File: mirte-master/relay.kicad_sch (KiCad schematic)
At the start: 2 parts, among them J17 NO relay contacts, J19 relay

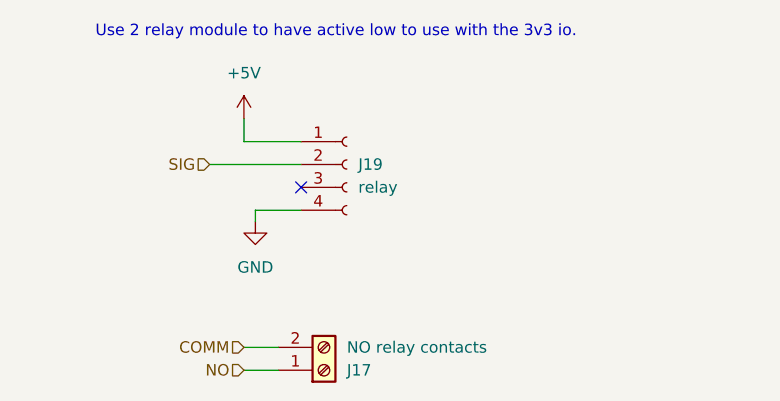
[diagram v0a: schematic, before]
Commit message: add kerco/elcos
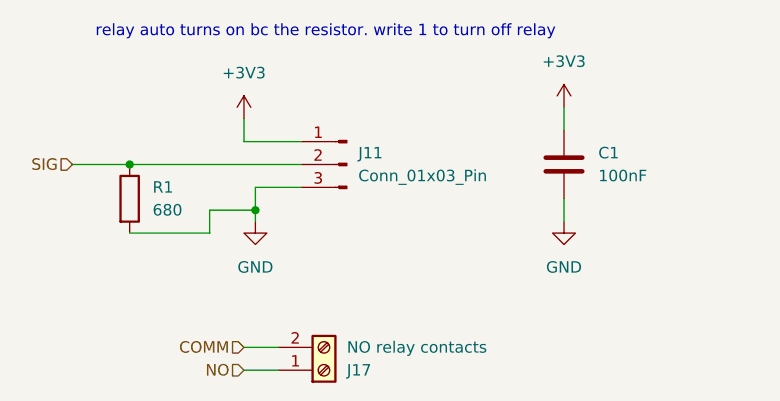
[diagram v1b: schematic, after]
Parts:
- removed J19: relay, Connector_JST:JST_XH_B4B-XH-A_1x04_P2.50mm_Vertical, symbol Connector:Conn_01x04_Socket
- added C1: 100nF, Capacitor_SMD:C_0805_2012Metric, symbol Device:C
- added J11: Conn_01x03_Pin, Connector_PinHeader_2.54mm:PinHeader_1x03_P2.54mm_Vertical, symbol Connector:Conn_01x03_Pin
- added R1: 680, Resistor_SMD:R_0805_2012Metric, symbol Device:R
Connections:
- net GND: now also C1.2, J11.3 (Pin_3), R1.2
- net SIG: now also J11.2 (Pin_2), R1.1
- new net +3V3: C1.1, J11.1 (Pin_1)
- no-connect marks 1 -> 0
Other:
- note added: "relay auto turns on bc the resistor. write 1 to turn off relay"
- note removed: "Use 2 relay module to have active low to use with the 3v3 io."
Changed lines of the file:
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@@
 (kicad_sch (version 20230121) (generator eeschema)
   (paper "A4")
-  (no_connect (at 101.6 67.31))
+  (junction (at 82.55 64.77) (diameter 0) (color 0 0 0 0)
+  )
+  (junction (at 96.52 69.85) (diameter 0) (color 0 0 0 0)
+  )
+  (wire (pts (xy 96.52 69.85) (xy 91.44 69.85))
+    (stroke (width 0) (type default))
+  )
   (wire (pts (xy 96.52 71.12) (xy 96.52 69.85))
     (stroke (width 0) (type default))
@@
     (stroke (width 0) (type default))
   )
-  (wire (pts (xy 96.52 69.85) (xy 101.6 69.85))
+  (wire (pts (xy 82.55 64.77) (xy 101.6 64.77))
+    (stroke (width 0) (type default))
+  )
+  (wire (pts (xy 130.81 58.42) (xy 130.81 60.96))
     (stroke (width 0) (type default))
   )
@@
     (stroke (width 0) (type default))
   )
-  (wire (pts (xy 91.44 64.77) (xy 101.6 64.77))
+  (wire (pts (xy 130.81 68.58) (xy 130.81 71.12))
+    (stroke (width 0) (type default))
+  )
+  (wire (pts (xy 91.44 69.85) (xy 91.44 72.39))
+    (stroke (width 0) (type default))
+  )
+  (wire (pts (xy 91.44 72.39) (xy 82.55 72.39))
+    (stroke (width 0) (type default))
+  )
+  (wire (pts (xy 76.2 64.77) (xy 82.55 64.77))
     (stroke (width 0) (type default))
   )
@@
     (stroke (width 0) (type default))
   )
+  (wire (pts (xy 96.52 69.85) (xy 96.52 67.31))
+    (stroke (width 0) (type default))
+  )
   (wire (pts (xy 95.25 85.09) (xy 99.06 85.09))
     (stroke (width 0) (type default))
   )
-  (text "Use 2 relay module to have active low to use with the 3v3 io."
+  (wire (pts (xy 96.52 67.31) (xy 101.6 67.31))
+    (stroke (width 0) (type default))
+  )
+  (text "relay auto turns on bc the resistor. write 1 to turn off relay"
     (at 78.74 50.8 0)
     (effects (font (size 1.27 1.27)) (justify left bottom))
@@
     (effects (font (size 1.27 1.27)) (justify right))
   )
-  (hierarchical_label "SIG" (shape input) (at 91.44 64.77 180) (fields_autoplaced)
+  (hierarchical_label "SIG" (shape input) (at 76.2 64.77 180) (fields_autoplaced)
     (effects (font (size 1.27 1.27)) (justify right))
+  )
+  (symbol (lib_id "Connector:Conn_01x03_Pin") (at 106.68 64.77 0) (mirror y) (unit 1)
+    (in_bom yes) (on_board yes) (dnp no) (fields_autoplaced)
+    (property "Reference" "J11" (at 107.95 63.5 0)
+      (effects (font (size 1.27 1.27)) (justify right))
+    )
+    (property "Value" "Conn_01x03_Pin" (at 107.95 66.04 0)
+      (effects (font (size 1.27 1.27)) (justify right))
+    )
+    (property "Footprint" "Connector_PinHeader_2.54mm:PinHeader_1x03_P2.54mm_Vertical" (at 106.68 64.77 0)
+      (effects (font (size 1.27 1.27)) hide)
+    )
+    (property "Datasheet" "~" (at 106.68 64.77 0)
+      (effects (font (size 1.27 1.27)) hide)
+    )
+    (pin "2")
+    (pin "3")
+    (pin "1")
+    (instances
+      (project "mirte-master"
+        (path "/19794465-0368-488c-958e-83b02754ebd6/17ebe4c8-09bb-4699-976c-396d27e4a3f5/544a16a8-9ef3-43b3-aa0f-4bd972816cae/d3337f2d-26a9-4529-9bfc-380e6deefc08"
+          (reference "J11") (unit 1)
+        )
+      )
+    )
+  )
+  (symbol (lib_id "power:GND") (at 130.81 71.12 0) (unit 1)
+    (in_bom yes) (on_board yes) (dnp no)
+    (property "Reference" "#PWR066" (at 130.81 77.47 0)
+      (effects (font (size 1.27 1.27)) hide)
+    )
+    (property "Value" "GND" (at 130.81 76.2 0)
+      (effects (font (size 1.27 1.27)))
+    )
+    (property "Footprint" "" (at 130.81 71.12 0)
+      (effects (font (size 1.27 1.27)) hide)
+    )
+    (property "Datasheet" "" (at 130.81 71.12 0)
+      (effects (font (size 1.27 1.27)) hide)
+    )
+    (pin "1")
+    (instances
+      (project "mirte-master"
+        (path "/19794465-0368-488c-958e-83b02754ebd6/17ebe4c8-09bb-4699-976c-396d27e4a3f5/544a16a8-9ef3-43b3-aa0f-4bd972816cae/d3337f2d-26a9-4529-9bfc-380e6deefc08"
+          (reference "#PWR066") (unit 1)
+        )
+      )
+    )
+  )
+  (symbol (lib_id "Device:C") (at 130.81 64.77 0) (unit 1)
+    (in_bom yes) (on_board yes) (dnp no) (fields_autoplaced)
+    (property "Reference" "C1" (at 134.62 63.5 0)
+      (effects (font (size 1.27 1.27)) (justify left))
+    )
+    (property "Value" "100nF" (at 134.62 66.04 0)
+      (effects (font (size 1.27 1.27)) (justify left))
+    )
+    (property "Footprint" "Capacitor_SMD:C_0805_2012Metric" (at 131.7752 68.58 0)
+      (effects (font (size 1.27 1.27)) hide)
+    )
+    (property "Datasheet" "~" (at 130.81 64.77 0)
+      (effects (font (size 1.27 1.27)) hide)
+    )
+    (pin "2")
+    (pin "1")
+    (instances
+      (project "mirte-master"
+        (path "/19794465-0368-488c-958e-83b02754ebd6/17ebe4c8-09bb-4699-976c-396d27e4a3f5"
+          (reference "C1") (unit 1)
+        )
+        (path "/19794465-0368-488c-958e-83b02754ebd6/17ebe4c8-09bb-4699-976c-396d27e4a3f5/544a16a8-9ef3-43b3-aa0f-4bd972816cae/d3337f2d-26a9-4529-9bfc-380e6deefc08"
+          (reference "C4") (unit 1)
+        )
+      )
+    )
   )
   (symbol (lib_id "Connector:Screw_Terminal_01x02") (at 104.14 87.63 0) (mirror x) (unit 1)
@@
     )
   )
-  (symbol (lib_id "power:+5V") (at 95.25 59.69 0) (unit 1)
-    (in_bom yes) (on_board yes) (dnp no) (fields_autoplaced)
-    (property "Reference" "#PWR013" (at 95.25 63.5 0)
-      (effects (font (size 1.27 1.27)) hide)
-    )
-    (property "Value" "+5V" (at 95.25 54.61 0)
+  (symbol (lib_id "power:+3V3") (at 95.25 59.69 0) (unit 1)
+    (in_bom yes) (on_board yes) (dnp no) (fields_autoplaced)
+    (property "Reference" "#PWR010" (at 95.25 63.5 0)
+      (effects (font (size 1.27 1.27)) hide)
+    )
+    (property "Value" "+3V3" (at 95.25 54.61 0)
       (effects (font (size 1.27 1.27)))
     )
@@
       (project "mirte-master"
         (path "/19794465-0368-488c-958e-83b02754ebd6/17ebe4c8-09bb-4699-976c-396d27e4a3f5/544a16a8-9ef3-43b3-aa0f-4bd972816cae/d3337f2d-26a9-4529-9bfc-380e6deefc08"
-          (reference "#PWR013") (unit 1)
+          (reference "#PWR010") (unit 1)
         )
       )
@@
     )
   )
-  (symbol (lib_id "Connector:Conn_01x04_Socket") (at 106.68 64.77 0) (unit 1)
-    (in_bom yes) (on_board yes) (dnp no) (fields_autoplaced)
-    (property "Reference" "J19" (at 107.95 64.77 0)
-      (effects (font (size 1.27 1.27)) (justify left))
-    )
-    (property "Value" "relay" (at 107.95 67.31 0)
-      (effects (font (size 1.27 1.27)) (justify left))
-    )
-    (property "Footprint" "Connector_JST:JST_XH_B4B-XH-A_1x04_P2.50mm_Vertical" (at 106.68 64.77 0)
-      (effects (font (size 1.27 1.27)) hide)
-    )
-    (property "Datasheet" "~" (at 106.68 64.77 0)
-      (effects (font (size 1.27 1.27)) hide)
-    )
-    (property "LCSC" "C144395" (at 107.95 64.77 0)
-      (effects (font (size 1.27 1.27)) hide)
-    )
-    (pin "1")
-    (pin "2")
-    (pin "4")
-    (pin "3")
-    (instances
-      (project "mirte-master"
-        (path "/19794465-0368-488c-958e-83b02754ebd6/17ebe4c8-09bb-4699-976c-396d27e4a3f5/544a16a8-9ef3-43b3-aa0f-4bd972816cae/d3337f2d-26a9-4529-9bfc-380e6deefc08"
-          (reference "J19") (unit 1)
-        )
-      )
+  (symbol (lib_id "Device:R") (at 82.55 68.58 0) (unit 1)
+    (in_bom yes) (on_board yes) (dnp no) (fields_autoplaced)
+    (property "Reference" "R1" (at 85.09 67.31 0)
+      (effects (font (size 1.27 1.27)) (justify left))
+    )
+    (property "Value" "680" (at 85.09 69.85 0)
+      (effects (font (size 1.27 1.27)) (justify left))
+    )
+    (property "Footprint" "Resistor_SMD:R_0805_2012Metric" (at 80.772 68.58 90)
+      (effects (font (size 1.27 1.27)) hide)
+    )
+    (property "Datasheet" "~" (at 82.55 68.58 0)
+      (effects (font (size 1.27 1.27)) hide)
+    )
+    (pin "2")
+    (pin "1")
+    (instances
+      (project "mirte-master"
+        (path "/19794465-0368-488c-958e-83b02754ebd6/17ebe4c8-09bb-4699-976c-396d27e4a3f5/544a16a8-9ef3-43b3-aa0f-4bd972816cae/d3337f2d-26a9-4529-9bfc-380e6deefc08"
+          (reference "R1") (unit 1)
+        )
+      )
+    )
+  )
+  (symbol (lib_id "power:+3V3") (at 130.81 58.42 0) (unit 1)
+    (in_bom yes) (on_board yes) (dnp no) (fields_autoplaced)
+    (property "Reference" "#PWR065" (at 130.81 62.23 0)
+      (effects (font (size 1.27 1.27)) hide)
+    )
+    (property "Value" "+3V3" (at 130.81 53.34 0)
+      (effects (font (size 1.27 1.27)))
+    )
+    (property "Footprint" "" (at 130.81 58.42 0)
+      (effects (font (size 1.27 1.27)) hide)
+    )
+    (property "Datasheet" "" (at 130.81 58.42 0)
+      (effects (font (size 1.27 1.27)) hide)
+    )
+    (pin "1")
+    (instances
+      (project "mirte-master"
+        (path "/19794465-0368-488c-958e-83b02754ebd6/17ebe4c8-09bb-4699-976c-396d27e4a3f5/544a16a8-9ef3-43b3-aa0f-4bd972816cae/d3337f2d-26a9-4529-9bfc-380e6deefc08"
+          (reference "#PWR065") (unit 1)
+        )
+      )

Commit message: mirte master parts jclpcb fixed
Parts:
- removed J17: NO relay contacts, TerminalBlock_Phoenix:TerminalBlock_Phoenix_PT-1,5-2-5.0-H_1x02_P5.00mm_Horizontal, symbol Connector:Screw_Terminal_01x02
- added J23: sc, easyeda:CONN-TH_XY126V-5.0-2P, symbol Connector:Screw_Terminal_01x02
- C1: LCSC (none) -> C49678
- J11: footprint Connector_PinHeader_2.54mm:PinHeader_1x03_P2.54mm_Vertical -> Connector_JST:JST_XH_B3B-XH-A_1x03_P2.50mm_Vertical; LCSC (none) -> C144394
- R1: LCSC (none) -> C17798
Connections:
- net COMM: now also J23.1 (Pin_1)
- net NO: now also J23.2 (Pin_2)
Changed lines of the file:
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@@
       (effects (font (size 1.27 1.27)) (justify right))
     )
-    (property "Footprint" "Connector_PinHeader_2.54mm:PinHeader_1x03_P2.54mm_Vertical" (at 106.68 64.77 0)
+    (property "Footprint" "Connector_JST:JST_XH_B3B-XH-A_1x03_P2.50mm_Vertical" (at 106.68 64.77 0)
       (effects (font (size 1.27 1.27)) hide)
     )
     (property "Datasheet" "~" (at 106.68 64.77 0)
+      (effects (font (size 1.27 1.27)) hide)
+    )
+    (property "LCSC" "C144394" (at 106.68 64.77 0)
       (effects (font (size 1.27 1.27)) hide)
     )
@@
       (effects (font (size 1.27 1.27)) hide)
     )
+    (property "LCSC" "C49678" (at 130.81 64.77 0)
+      (effects (font (size 1.27 1.27)) hide)
+    )
     (pin "2")
     (pin "1")
@@
         (path "/19794465-0368-488c-958e-83b02754ebd6/17ebe4c8-09bb-4699-976c-396d27e4a3f5/544a16a8-9ef3-43b3-aa0f-4bd972816cae/d3337f2d-26a9-4529-9bfc-380e6deefc08"
           (reference "C4") (unit 1)
-        )
-      )
-    )
-  )
-  (symbol (lib_id "Connector:Screw_Terminal_01x02") (at 104.14 87.63 0) (mirror x) (unit 1)
-    (in_bom yes) (on_board yes) (dnp no)
-    (property "Reference" "J17" (at 106.68 87.63 0)
-      (effects (font (size 1.27 1.27)) (justify left))
-    )
-    (property "Value" "NO relay contacts" (at 106.68 85.09 0)
-      (effects (font (size 1.27 1.27)) (justify left))
-    )
-    (property "Footprint" "TerminalBlock_Phoenix:TerminalBlock_Phoenix_PT-1,5-2-5.0-H_1x02_P5.00mm_Horizontal" (at 104.14 87.63 0)
-      (effects (font (size 1.27 1.27)) hide)
-    )
-    (property "Datasheet" "~" (at 104.14 87.63 0)
-      (effects (font (size 1.27 1.27)) hide)
-    )
-    (property "LCSC" "C557646" (at 106.68 87.63 0)
-      (effects (font (size 1.27 1.27)) hide)
-    )
-    (pin "2")
-    (pin "1")
-    (instances
-      (project "mirte-master"
-        (path "/19794465-0368-488c-958e-83b02754ebd6/17ebe4c8-09bb-4699-976c-396d27e4a3f5/544a16a8-9ef3-43b3-aa0f-4bd972816cae/d3337f2d-26a9-4529-9bfc-380e6deefc08"
-          (reference "J17") (unit 1)
         )
       )
@@
         (path "/19794465-0368-488c-958e-83b02754ebd6/17ebe4c8-09bb-4699-976c-396d27e4a3f5/544a16a8-9ef3-43b3-aa0f-4bd972816cae/d3337f2d-26a9-4529-9bfc-380e6deefc08"
           (reference "#PWR010") (unit 1)
+        )
+      )
+    )
+  )
+  (symbol (lib_id "Connector:Screw_Terminal_01x02") (at 104.14 85.09 0) (unit 1)
+    (in_bom yes) (on_board yes) (dnp no) (fields_autoplaced)
+    (property "Reference" "J23" (at 106.68 85.09 0)
+      (effects (font (size 1.27 1.27)) (justify left))
+    )
+    (property "Value" "sc" (at 106.68 87.63 0)
+      (effects (font (size 1.27 1.27)) (justify left))
+    )
+    (property "Footprint" "easyeda:CONN-TH_XY126V-5.0-2P" (at 104.14 85.09 0)
+      (effects (font (size 1.27 1.27)) hide)
+    )
+    (property "Datasheet" "~" (at 104.14 85.09 0)
+      (effects (font (size 1.27 1.27)) hide)
+    )
+    (property "LCSC" "C557646" (at 104.14 85.09 0)
+      (effects (font (size 1.27 1.27)) hide)
+    )
+    (pin "2")
+    (pin "1")
+    (instances
+      (project "mirte-master"
+        (path "/19794465-0368-488c-958e-83b02754ebd6/17ebe4c8-09bb-4699-976c-396d27e4a3f5/cd5c3f96-e789-467d-9a0a-1e1e5a42c039"
+          (reference "J23") (unit 1)
+        )
+        (path "/19794465-0368-488c-958e-83b02754ebd6/17ebe4c8-09bb-4699-976c-396d27e4a3f5/1f6ba3bd-b93c-4e80-aba0-1409dab869f7"
+          (reference "J13") (unit 1)
+        )
+        (path "/19794465-0368-488c-958e-83b02754ebd6/17ebe4c8-09bb-4699-976c-396d27e4a3f5/544a16a8-9ef3-43b3-aa0f-4bd972816cae/d3337f2d-26a9-4529-9bfc-380e6deefc08"
+          (reference "J17") (unit 1)
         )
       )
@@
       (effects (font (size 1.27 1.27)) hide)
     )
+    (property "LCSC" "C17798" (at 82.55 68.58 0)
+      (effects (font (size 1.27 1.27)) hide)
+    )

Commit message: mirte-master schematic cleanup and readabilityimprovements
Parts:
- renumbered C1 to C4, J23 to J21
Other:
- title: (none) -> ${PROJECTNAME}
